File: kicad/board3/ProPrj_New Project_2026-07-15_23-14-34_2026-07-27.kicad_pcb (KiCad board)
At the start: 4 copper layers, 250 x 50 mm, 144 parts, among them P1 WJ500V-5.08-2P, P2 WJ500V-5.08-2P, Q1 AO4406A, Q2 AO4406A, SW1 HX TS4538CJ 250gf 009, SW2 HX TS4538CJ 250gf 009, SW3 HX TS4538CJ 250gf 009, SW4 HX TS4538CJ 250gf 009, SW6 HX TS4538CJ 250gf 009, SW7 HX TS4538CJ 250gf 009, U1 STM32H755ZIT6, U10 ULN2803A, U2 W25Q512JVEIQ TR, U3 TPS563201DDCR, U4 CH224K, U5 LM74700QDBVRQ1, U6 LM74700QDBVRQ1, U7 FM24CL64B-GTR, U8 TJA1051T/3/1J, U9 TJA1051T/3/1J, X1 25MHz

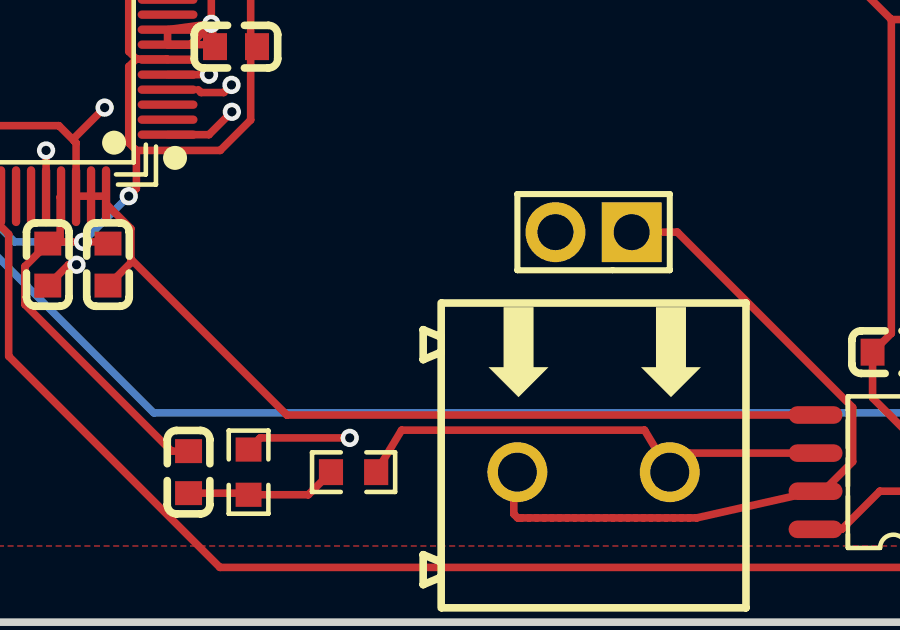
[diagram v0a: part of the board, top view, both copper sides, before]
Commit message: fix(kicad): cut CAN1_TERM's +5V plane slot from 9.70 mm to 1.51 mm
The U6 writeup called this the twin of the CAN2 jumper stub and "a one-line
change". That was wrong, and the reason is worth recording: CAN2's stub moved
wholesale to the bottom layer because both endpoints were through-hole and the
corridor was empty. CAN1_TERM's endpoints, R10.1 and H1.2, are separated by two
full-width barriers at almost the same latitude -- +3V3 on the top at y=128.095
and CAN1_RX on the bottom at y=128.023 -- so neither outer layer can carry the
crossing. The import used an inner layer because that is the only layer that can.

Going around is possible and not worth it: either a ~20 mm detour east of U8, or
a squeeze through the 0.51 mm gap between CAN1_RX's via and the GND bus at
(155.7,122.3), which would leave 0.05 mm of margin on a board headed for fab.

What is worth it is noticing that only the CROSSING has to be on the plane. The
stub now runs the bottom layer from H1.2 to a new via at (166.872,127.350), hops
1.508 mm across both barriers on Inner2, and rejoins the existing via at
(166.872,128.858). The slot in the +5V plane shrinks 84%, at the cost of one via
on a DC termination jumper leg where length and vias are electrically free.

Measured: 13.739 mm, 2 vias, {Bottom 8.698, Top 3.533, Inner2 1.508}. DRC 35
against the real rules, NEW = 0 over the 41-violation import baseline, airwires
0, and exactly one net changed.

For scale on what the slot was costing: the only bottom-layer trace crossing it
was CAN1_RX, at 1 Mbps. This was cheap hygiene, not a rescue.

Co-Authored-By: Claude Opus 5 (1M context) <noreply@anthropic.com>
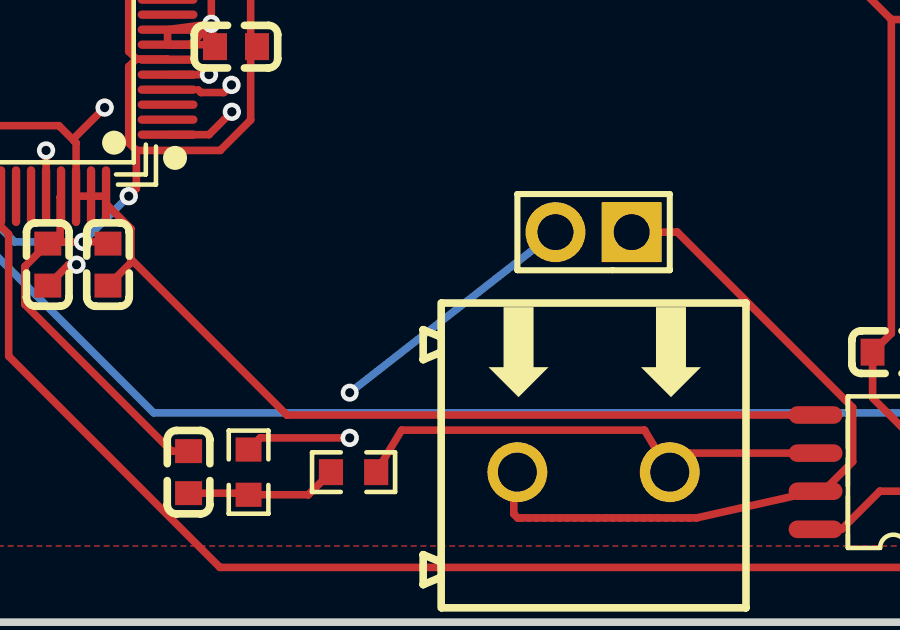
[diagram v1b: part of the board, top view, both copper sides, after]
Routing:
- net /CAN1_TERM: track 13.2 -> 13.7 mm, vias 1 -> 2
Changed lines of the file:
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@@
+	)
+	(via
+		(at 166.872 127.35)
+		(size 0.6)
+		(drill 0.3)
+		(layers "F.Cu" "B.Cu")
+		(net "/CAN1_TERM")
 	)
 	(via
@@
 	)
 	(segment
-		(start 173.73 122)
-		(end 166.872 128.858)
+		(start 166.872 127.35)
+		(end 173.73 122)
+		(width 0.254)
+		(layer "B.Cu")
+		(net "/CAN1_TERM")
+	)
+	(segment
+		(start 166.872 128.858)
+		(end 166.872 127.35)
 		(width 0.254)
 		(layer "In2.Cu")

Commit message: feat(kicad): give U2 and U4 thermal vias and the board fiducials it never had
U7. Nine tented vias into U2's thermal pad, five into U4's, three fiducials on
F.Cu. FD-001 clears, both TV-001 findings drop from warning to info, DRC holds at
35 against the real rules with NEW = 0 over the 41-violation import baseline, and
airwires stay at 0.

The plan expected U2 to have 5 vias already. It had none -- the reviewer's count
was picking up vias near the part, not in the pad. U4 had none as stated. All 14
are 0.6/0.3, which is a 0.15 mm annular ring and exactly JLC's minimum; the
0.45 mm via that also fits U4's smaller pad leaves 0.075 mm and was rejected.

A plain 3x3 grid would have shorted three of U2's vias, and nothing on the top
layer would have warned you. U6 put QSPI_IO2 and QSPI_IO1 under that thermal pad
on the bottom, and MOSI_R_MCU crosses Inner1 diagonally right through it. So the
positions come from a clearance-aware grid search over all four copper layers
with a 0.5 mm hole-to-hole floor, not from a hand-drawn pattern. This is trap 2
in kicad_handroute.py stated again in a different accent: on this board, "the
outer layers are clear here" is not evidence.

Tenting is the half of TV-001 that is easy to skip -- an untented via in a
thermal pad wicks solder during reflow and leaves a void under the pad -- so
kicad_handroute.py grew a "tented" flag and all 14 carry (tenting (front yes)
(back yes)).

Fiducials went to the three clearest points on the top layer, found by scanning
for maximum bare radius: west-north (2.33 mm), centre-south (4.51) and east-south
(9.13). The triangle is deliberately asymmetric so a vision system can detect a
180-degree flip. They are board_only, so Update PCB from Schematic will not
delete parts that have no symbol, and excluded from BOM and CPL.

Two reviewer defects surfaced, neither of them board defects:

kicad-happy cannot read KiCad 10's via tenting. It still reports "13 via(s) are
not tented" for vias the file marks tented and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
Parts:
- added FID1: Fiducial_1mm_Mask2mm, Fiducial_1mm_Mask2mm, F.Cu at (40.5, 93.8)
- added FID2: Fiducial_1mm_Mask2mm, Fiducial_1mm_Mask2mm, F.Cu at (153.2, 130.5)
- added FID3: Fiducial_1mm_Mask2mm, Fiducial_1mm_Mask2mm, F.Cu at (259.0, 126.0)
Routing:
- net /GND: vias 20 -> 34

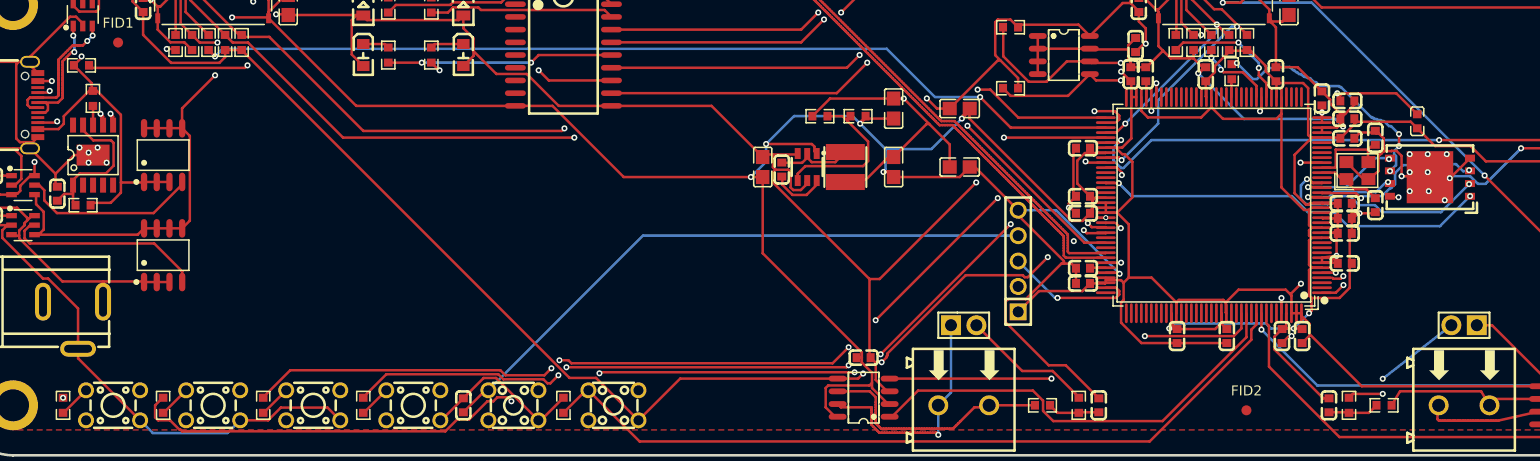
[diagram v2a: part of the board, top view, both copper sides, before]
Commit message: fix(kicad): get the vias out of the pads, and fix the four blind spots that hid them
U7 follow-up. Running kicad-happy for U7's thermal findings turned up something
DRC and my own measurements had both missed: SIX QSPI escape vias sitting inside
U2's SMD pads, put there by U6's bottom-layer reroute. An unplugged via in an SMD
pad wicks solder off the joint during reflow -- a 0.3 mm barrel holds more than a
small pad's entire paste deposit -- and these were the flash's six signal pins.

Why nothing caught it is the durable part. Via-in-pad is not a DRC rule, so
kicad_verify stayed green at 35 with NEW = 0. It is not a length, via-count or
layer fact either, so kicad_measure -- which is what U6's verification leaned on
-- could not see it. "DRC clean and measured" is not "assemblable".

U6's crystal fix had to go back too, and the reason is worth recording. The only
lane wide enough to escape U2's west pads is the 0.96 mm between the Inner2
keepout edge (x=166.129) and the pads (x=167.090), and moving X1 0.5 mm east had
pushed the crystal's case-ground guard into it. That guard is not redundant --
deleting it leaves an airwire, tested. With X1 moved east by d, the QSPI escape
needs d <= 0.149 and OSC_OUT's corridor needs d >= 0.214, so the two fixes cannot
both exist. A starved joint on the flash beats an oscillator's loop area, so both
went back to the imported geometry, with the analysis preserved in
kicad_netclass.json under $walked_back for whoever re-plans that corner.

R6 and R8 are therefore NOT met, and the plan says so. Kept from U6: the CAN
fixes, the USB symmetry fix, and CAN1_TERM's plane slot at 1.51 mm.

The one via that could not leave its pad is U1.93 (BTN1), boxed in by a 0.5 mm
pitch QFP pad row, a +3V3 diagonal 1.6 mm east and a GND trace 0.295 mm west that
is also load-bearing. Its hard breach was the annular ring: 0.10 mm against JLC's
published 0.15 mm minimum. The neighbours cap the diameter at 0.517 mm, so the
drill shrank instead -- 0.5/0.2 gi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
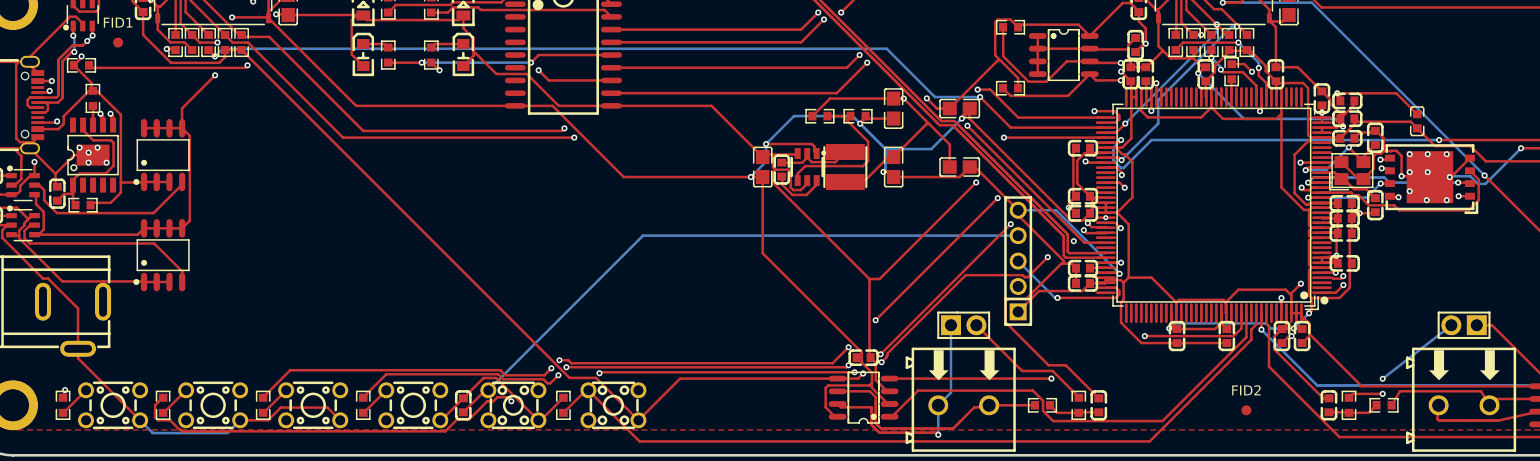
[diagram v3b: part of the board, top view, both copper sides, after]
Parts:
- moved X1 0.50 mm to (163.8, 106.5)
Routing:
- net /QSPI_IO1: track 23.1 -> 18.0 mm
- net /QSPI_CLK: track 24.8 -> 21.7 mm, vias 4 -> 2
- net /QSPI_IO2: track 17.2 -> 20.1 mm, vias 2 -> 0
- net /OSC_OUT: track 8.34 -> 11.2 mm, vias 0 -> 2
- net /GND: track 868.4 -> 866.1 mm
- net /QSPI_IO0: track 10.7 -> 12.5 mm

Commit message: feat(kicad): land R49 on the board, ground the mounting holes, align the top pour
Three things the board needed, all verified against the same bar: 36 DRC
violations, NEW = 0 over the 41-violation import baseline, 0 airwires.

R49 (U3's NRST pull-up) crossed from the schematic in Kevin's sync and arrived
parked at (1.52,0.74), off the board, because the placement dialog was escaped.
It now sits at (75.0,122.5) in the reset cluster, ~8 mm north of C46, at a point
measured clear by 3.87 mm. Routing it by hand failed and is worth recording:
the obvious descent at x=77.2 crossed BTN4 and two GND runs, which DRC caught as
2 tracks_crossing and a short. That pocket has BTN2, BTN4 and the reset GND
returns threading through it and is not eyeball-routable. KiCadRoutingTools
threaded it in 5.6 mm of NRST and 4.8 mm of +3V3, and a net-level diff confirms
it only ADDED copper -- two nets changed, both grew, no other net touched.

The four mounting holes are now on GND. They are Pad_e672/673/674/675: single
PTH pads, 3.2 mm drill for M3 with a 5 mm annulus, at the board corners, and
until now on no net at all -- four isolated copper islands that would take
whatever potential their standoffs gave them, on a board going into a metal
chassis. Note where that net assignment lives: these footprints have no
schematic symbol, so nothing upstream asserts it. The sync leaves them alone
(verified) but a future run with "delete footprints with no symbols" ticked
would remove the holes entirely, which is worse than the net. Mounting-hole
symbols in the schematic are the durable fix.

The Top GND pour was misaligned, spotted by eye in the editor. It is the same
76-point rounded rectangle as the other three zones, translated by
(+0.867,-2.539) mm -- so it overhung the top and right edges, where the fill
clipped it harmlessly, and fell 2.67 mm short along the bottom and 0.99 mm short
on the left, leaving strips of board with no top-layer ground. Confirmed
byte-identical in 52586d4, the origin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
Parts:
- added R49: 10kΩ, ProPrj_New-easyedapro:R0603, F.Cu at (75.0, 122.5)
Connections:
- ? pad 1: (no net) -> /GND (x4)
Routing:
- net /NRST: track 95.8 -> 101.4 mm, vias 1 -> 2
- net /+3V3: track 563.1 -> 566.3 mm
